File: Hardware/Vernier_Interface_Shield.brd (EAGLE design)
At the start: 42 parts, among them U1 74HC4052SO, U2 LMV358

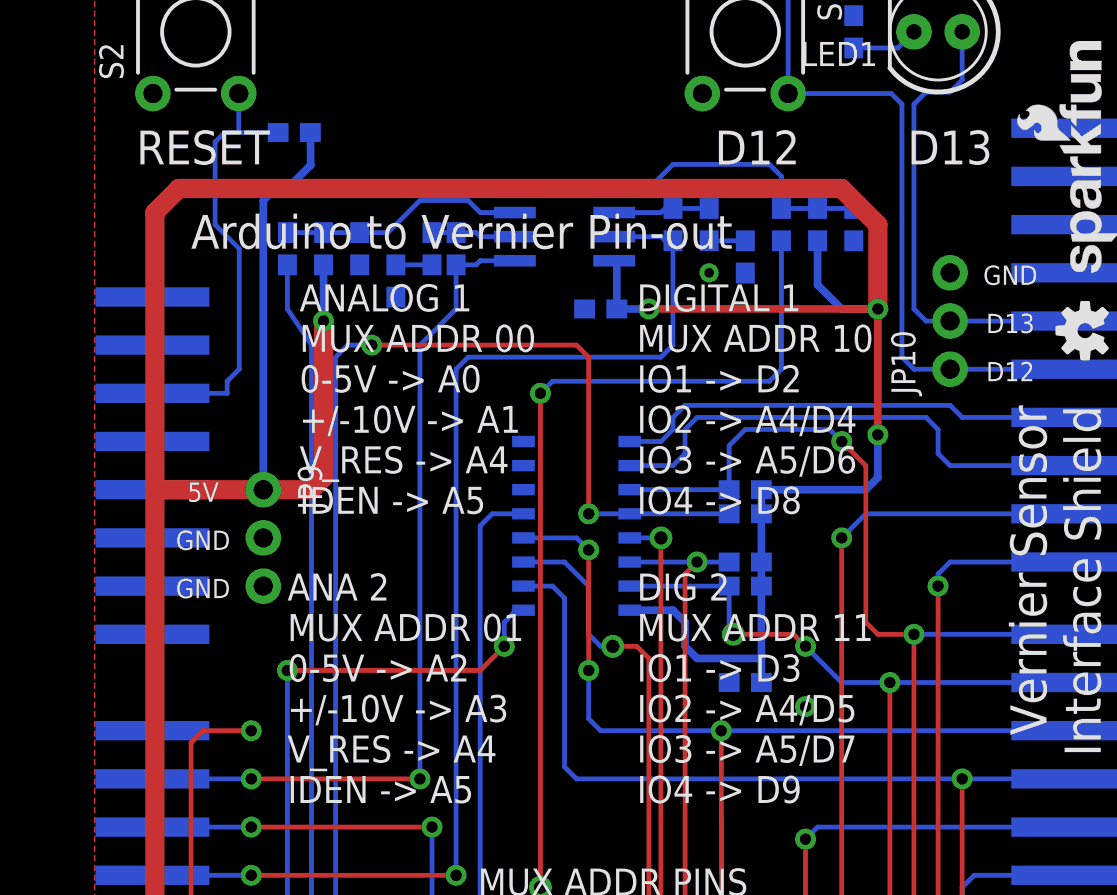
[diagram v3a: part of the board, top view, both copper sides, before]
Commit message: addtl clean-up: corrected resistor spacing
Corrected resistor spacing and cleaned-up resulting traces.
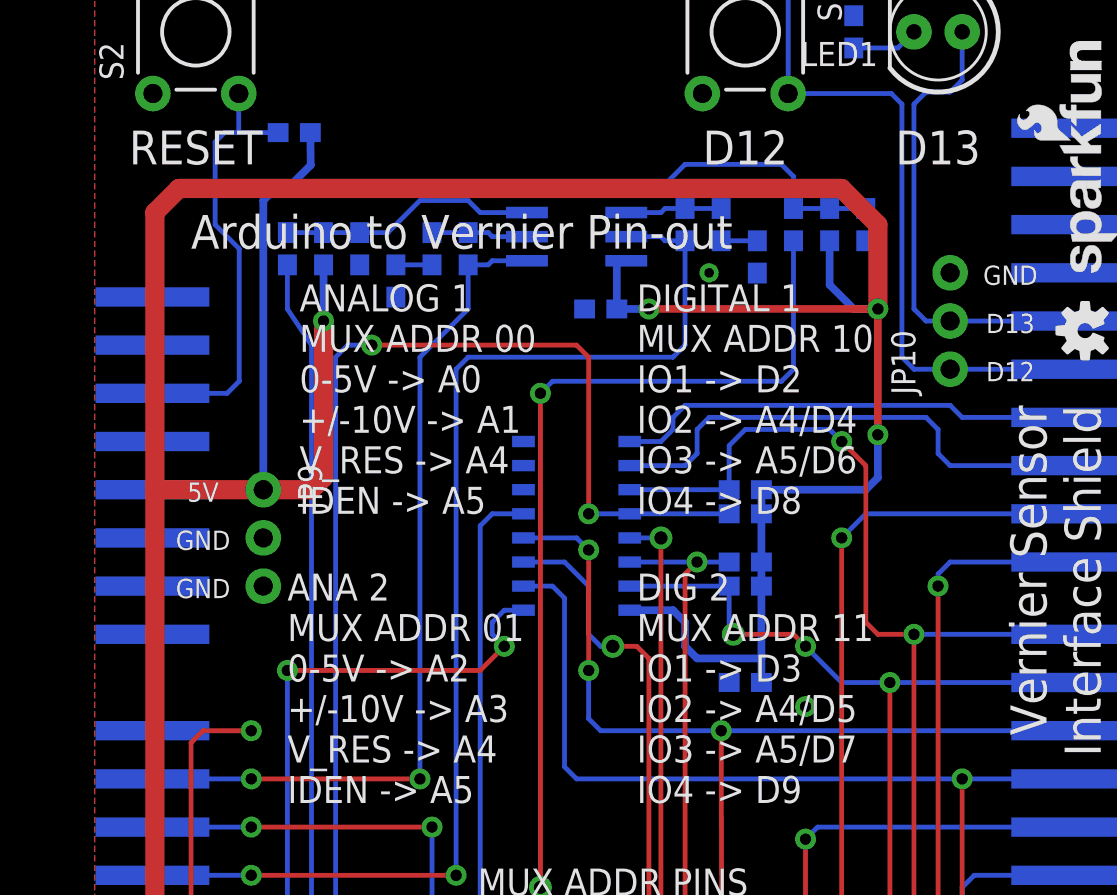
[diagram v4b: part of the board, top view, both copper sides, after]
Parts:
- moved R7 0.64 mm to (51.4, 62.2)
- moved R5 0.64 mm to (30.5, 61.0)
- moved R10 0.63 mm to (43.8, 62.2)
- moved R11 0.63 mm to (41.9, 62.2)
- moved R12 0.63 mm to (49.5, 62.2)
- moved R8 0.63 mm to (47.6, 62.2)
- moved R9 0.63 mm to (45.7, 60.5)
- moved U2 0.63 mm to (36.2, 62.2)
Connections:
- net AS1_VRES renamed N$24
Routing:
- net N$24: track 46.4 -> 47.3 mm
- net N$3: track 4.46 -> 5.09 mm
- net N$1: track 13.0 -> 13.6 mm
- net AS2_AN1: track 58.5 -> 59.1 mm
- net A3: track 64.0 -> 64.6 mm

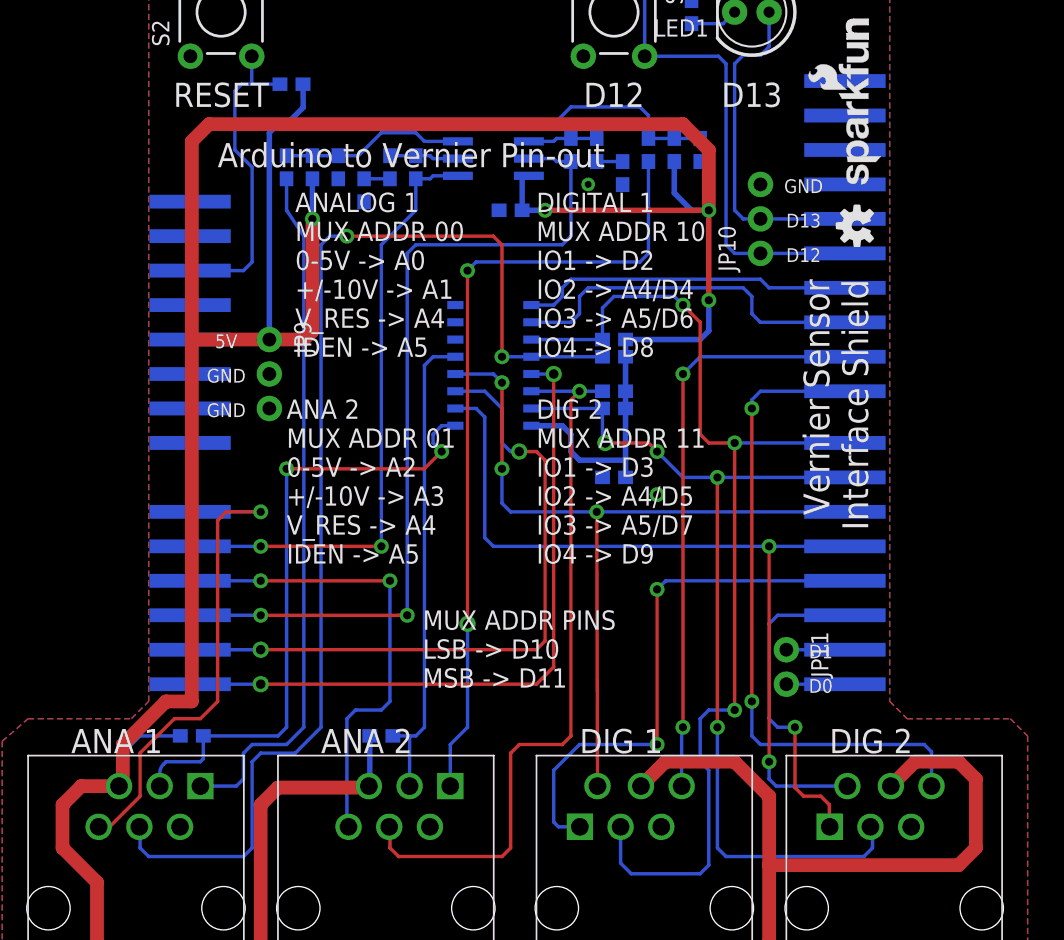
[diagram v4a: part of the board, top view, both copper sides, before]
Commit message: Updated footprints of BTA and BTD connectors
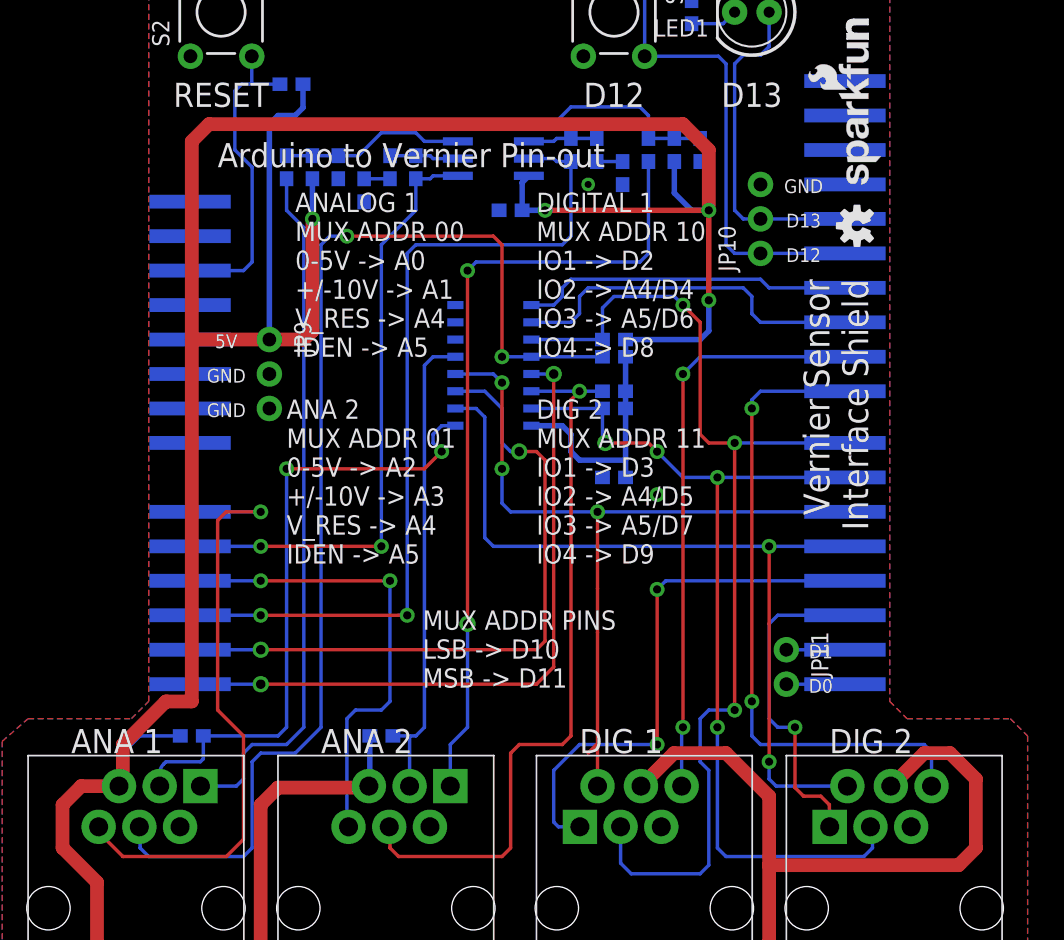
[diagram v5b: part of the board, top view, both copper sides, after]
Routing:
- net AS1_AN2: track 36.4 -> 45.3 mm
- net 5V: track 345.3 -> 346.6 mm
- net D2_IO2: track 58.4 -> 59.3 mm
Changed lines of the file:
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@@
 <setting verticaltext="up"/>
 </settings>
-<grid distance="0.025" unitdist="inch" unit="inch" style="lines" multiple="1" display="yes" altdistance="0.005" altunitdist="inch" altunit="inch"/>
+<grid distance="0.05" unitdist="inch" unit="inch" style="lines" multiple="1" display="yes" altdistance="0.005" altunitdist="inch" altunit="inch"/>
 <layers>
 <layer number="1" name="Top" color="4" fill="1" visible="yes" active="yes"/>
@@
 </class>
 </classes>
-<designrules name="SparkFun">
+<designrules name="SparkFun *">
 <description language="en">&lt;b&gt;EAGLE Design Rules&lt;/b&gt;
 &lt;p&gt;
@@
 <param name="dpGapFactor" value="2.5"/>
 <param name="checkGrid" value="0"/>
-<param name="checkAngle" value="0"/>
+<param name="checkAngle" value="1"/>
 <param name="checkFont" value="1"/>
 <param name="checkRestrict" value="1"/>
@@
 <wire x1="8.89" y1="15.635" x2="8.605" y2="15.35" width="0.254" layer="16"/>
 <wire x1="10.16" y1="19.05" x2="8.89" y2="17.78" width="0.254" layer="16"/>
-<wire x1="47.07" y1="15.35" x2="48.865" y2="17.145" width="1.016" layer="1"/>
-<wire x1="48.865" y1="17.145" x2="53.975" y2="17.145" width="1.016" layer="1"/>
-<wire x1="53.975" y1="17.145" x2="56.515" y2="14.605" width="1.016" layer="1"/>
+<wire x1="47.07" y1="15.35" x2="49.5" y2="17.78" width="1.016" layer="1"/>
+<wire x1="53.34" y1="17.78" x2="56.515" y2="14.605" width="1.016" layer="1"/>
 <wire x1="56.515" y1="14.605" x2="56.515" y2="9.525" width="1.016" layer="1"/>
 <wire x1="56.515" y1="9.525" x2="56.515" y2="3.81" width="1.016" layer="1"/>
-<wire x1="65.485" y1="15.35" x2="67.28" y2="17.145" width="1.016" layer="1"/>
-<wire x1="67.28" y1="17.145" x2="70.485" y2="17.145" width="1.016" layer="1"/>
-<wire x1="70.485" y1="17.145" x2="71.755" y2="15.875" width="1.016" layer="1"/>
+<wire x1="69.85" y1="17.78" x2="71.755" y2="15.875" width="1.016" layer="1"/>
 <wire x1="71.755" y1="15.875" x2="71.755" y2="10.795" width="1.016" layer="1"/>
 <wire x1="71.755" y1="10.795" x2="70.485" y2="9.525" width="1.016" layer="1"/>
@@
 <via x="52.07" y="57.785" extent="1-16" drill="0.6"/>
 <wire x1="13.12" y1="19.05" x2="10.16" y2="19.05" width="0.254" layer="16"/>
-<wire x1="22.165" y1="67.08" x2="22.183" y2="65.363" width="0.4064" layer="16"/>
-<wire x1="22.183" y1="65.363" x2="20.955" y2="64.135" width="0.4064" layer="16"/>
 <wire x1="22.86" y1="60.11" x2="22.86" y2="57.15" width="0.4064" layer="16"/>
 <wire x1="49.53" y1="61.38" x2="49.53" y2="59.055" width="0.4064" layer="16"/>
 <wire x1="49.53" y1="59.055" x2="50.8" y2="57.785" width="0.4064" layer="16"/>
 <wire x1="50.8" y1="57.785" x2="52.07" y2="57.785" width="0.4064" layer="16"/>
-<wire x1="38.315" y1="57.785" x2="38.315" y2="60.1862" width="0.4064" layer="16"/>
-<wire x1="38.315" y1="60.1862" x2="38.8112" y2="60.325" width="0.4064" layer="16"/>
 <wire x1="38.315" y1="57.785" x2="40.005" y2="57.785" width="0.4064" layer="16"/>
 <wire x1="50.165" y1="64.135" x2="52.07" y2="62.23" width="1.016" layer="1"/>
@@
 <wire x1="50.165" y1="64.135" x2="15.24" y2="64.135" width="1.016" layer="1"/>
 <wire x1="15.24" y1="64.135" x2="13.97" y2="62.865" width="1.016" layer="1"/>
-<wire x1="19.685" y1="63.5" x2="19.685" y2="48.26" width="0.4064" layer="16"/>
-<wire x1="20.955" y1="64.135" x2="20.32" y2="64.135" width="0.4064" layer="16"/>
-<wire x1="20.32" y1="64.135" x2="19.685" y2="63.5" width="0.4064" layer="16"/>
+<wire x1="19.685" y1="64.135" x2="19.685" y2="48.26" width="0.4064" layer="16"/>
 <wire x1="13.843" y1="48.26" x2="19.685" y2="48.26" width="0.4064" layer="16"/>
 <wire x1="13.97" y1="62.865" x2="13.97" y2="48.26" width="1.016" layer="1"/>
 <wire x1="13.97" y1="48.26" x2="19.685" y2="48.26" width="1.016" layer="1"/>
 <wire x1="13.97" y1="48.26" x2="13.97" y2="21.59" width="1.016" layer="1"/>
+<wire x1="53.34" y1="17.78" x2="49.5" y2="17.78" width="1.016" layer="1"/>
+<wire x1="67.945" y1="17.78" x2="69.85" y2="17.78" width="1.016" layer="1"/>
+<wire x1="65.485" y1="15.35" x2="65.515" y2="15.35" width="1.016" layer="1"/>
+<wire x1="65.515" y1="15.35" x2="67.945" y2="17.78" width="1.016" layer="1"/>
+<wire x1="22.165" y1="67.08" x2="22.165" y2="65.345" width="0.4064" layer="16"/>
+<wire x1="19.685" y1="64.135" x2="20.32" y2="64.77" width="0.4064" layer="16"/>
+<wire x1="20.32" y1="64.77" x2="21.59" y2="64.77" width="0.4064" layer="16"/>
+<wire x1="21.59" y1="64.77" x2="22.165" y2="65.345" width="0.4064" layer="16"/>
+<wire x1="38.315" y1="57.785" x2="38.315" y2="59.8288" width="0.4064" layer="16"/>
+<wire x1="38.315" y1="59.8288" x2="38.8112" y2="60.325" width="0.4064" layer="16"/>
 </signal>
 <signal name="3.3V">
@@
 <contactref element="JP5" pad="1"/>
 <wire x1="20.955" y1="60.11" x2="20.955" y2="57.785" width="0.254" layer="16"/>
-<wire x1="20.955" y1="57.785" x2="22.225" y2="55.88" width="0.254" layer="16"/>
-<wire x1="22.225" y1="55.88" x2="22.225" y2="19.685" width="0.254" layer="16"/>
+<wire x1="22.225" y1="56.515" x2="22.225" y2="19.685" width="0.254" layer="16"/>
 <wire x1="17.78" y1="15.875" x2="17.78" y2="17.78" width="0.254" layer="16"/>
 <wire x1="17.78" y1="17.78" x2="18.415" y2="18.415" width="0.254" layer="16"/>
@@
 <wire x1="14.605" y1="15.35" x2="17.255" y2="15.35" width="0.254" layer="16"/>
 <wire x1="17.255" y1="15.35" x2="17.78" y2="15.875" width="0.254" layer="16"/>
+<wire x1="22.225" y1="56.515" x2="20.955" y2="57.785" width="0.254" layer="16"/>
 </signal>
 <signal name="AS1_AUTOID">
@@
 <contactref element="JP5" pad="6"/>
 <contactref element="JP4" pad="6"/>
-<wire x1="7.105" y1="12.35" x2="7.905" y2="12.35" width="0.254" layer="1"/>
-<wire x1="7.905" y1="12.35" x2="10.16" y2="14.605" width="0.254" layer="1"/>
-<wire x1="10.16" y1="14.605" x2="10.16" y2="17.78" width="0.254" layer="1"/>
-<wire x1="10.16" y1="17.78" x2="12.7" y2="20.32" width="0.254" layer="1"/>
-<wire x1="12.7" y1="20.32" x2="14.605" y2="20.32" width="0.254" layer="1"/>
-<wire x1="14.605" y1="20.32" x2="15.875" y2="21.59" width="0.254" layer="1"/>
-<wire x1="15.875" y1="21.59" x2="15.875" y2="34.925" width="0.254" layer="1"/>
+<wire x1="15.875" y1="20.955" x2="15.875" y2="34.925" width="0.254" layer="1"/>
 <wire x1="15.875" y1="34.925" x2="16.51" y2="35.56" width="0.254" layer="1"/>
 <wire x1="16.51" y1="35.56" x2="19.05" y2="35.56" width="0.254" layer="1"/>
 <via x="19.05" y="35.56" extent="1-16" drill="0.6"/>
 <wire x1="19.05" y1="35.56" x2="13.843" y2="35.56" width="0.254" layer="16"/>
+<wire x1="15.875" y1="20.955" x2="17.78" y2="19.05" width="0.254" layer="1"/>
+<wire x1="17.78" y1="19.05" x2="17.78" y2="11.43" width="0.254" layer="1"/>
+<wire x1="17.78" y1="11.43" x2="16.51" y2="10.16" width="0.254" layer="1"/>
+<wire x1="16.51" y1="10.16" x2="8.89" y2="10.16" width="0.254" layer="1"/>
+<wire x1="7.105" y1="12.35" x2="7.105" y2="11.945" width="0.254" layer="1"/>
+<wire x1="7.105" y1="11.945" x2="8.89" y2="10.16" width="0.254" layer="1"/>
 </signal>
 <signal name="AS2_AN2">
@@
 <contactref element="JP2" pad="6"/>
 <contactref element="JP8" pad="2"/>
-<wire x1="62.103" y1="35.56" x2="43.815" y2="35.56" width="0.254" layer="16"/>
-<wire x1="43.815" y1="35.56" x2="37.465" y2="35.56" width="0.254" layer="16"/>
+<wire x1="62.103" y1="35.56" x2="43.87" y2="35.56" width="0.254" layer="16"/>
+<wire x1="43.87" y1="35.56" x2="37.465" y2="35.56" width="0.254" layer="16"/>
 <wire x1="37.465" y1="35.56" x2="36.83" y2="36.195" width="0.254" layer="16"/>
 <wire x1="36.83" y1="36.195" x2="36.83" y2="38.735" width="0.254" layer="16"/>
@@
 <wire x1="36.83" y1="45.085" x2="36.195" y2="45.72" width="0.254" layer="16"/>
 <wire x1="36.195" y1="45.72" x2="33.395" y2="45.72" width="0.254" layer="16"/>
-<wire x1="43.87" y1="35.505" x2="43.815" y2="35.56" width="0.254" layer="16"/>
-<via x="43.815" y="35.56" extent="1-16" drill="0.6"/>
-<wire x1="43.815" y1="35.56" x2="43.87" y2="15.35" width="0.254" layer="1"/>
+<wire x1="43.87" y1="35.505" x2="43.87" y2="35.56" width="0.254" layer="16"/>
+<via x="43.87" y="35.56" extent="1-16" drill="0.6"/>
+<wire x1="43.815" y1="18.415" x2="43.18" y2="17.78" width="0.254" layer="1"/>
+<wire x1="43.87" y1="15.35" x2="43.87" y2="26.67" width="0.254" layer="1"/>
+<wire x1="43.87" y1="26.67" x2="43.87" y2="29.9" width="0.254" layer="1"/>
+<wire x1="43.87" y1="35.56" x2="43.87" y2="29.9" width="0.254" layer="1"/>
+<wire x1="43.87" y1="15.35" x2="43.18" y2="17.78" width="0" layer="19" extent="1-1"/>
 </signal>
 <signal name="D2_IO1">
